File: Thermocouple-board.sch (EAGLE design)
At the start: 82 parts, among them J1 RJ45, J10 1X2-3.5MM, J11 1X2-3.5MM, J12 1X2-3.5MM, J13 1X2-3.5MM, J2 RJ45, J3 1981584-1, J4 2.1MMJACKTHM, J5 ST-LINK, J6 HEADER-1X3, J7 UART, SW1 PUSHBUTTON, SW2 PUSHBUTTON, U1 STM32F042K4, U10 MAX31855, U11 MAX31855, U12 MAX31855, U13 MAX31855, U20 EEPROM-I2C, U21 EEPROM-I2C, U30 ST3485, U31 ST3485, U40 LP298XS, Y1 8MHz

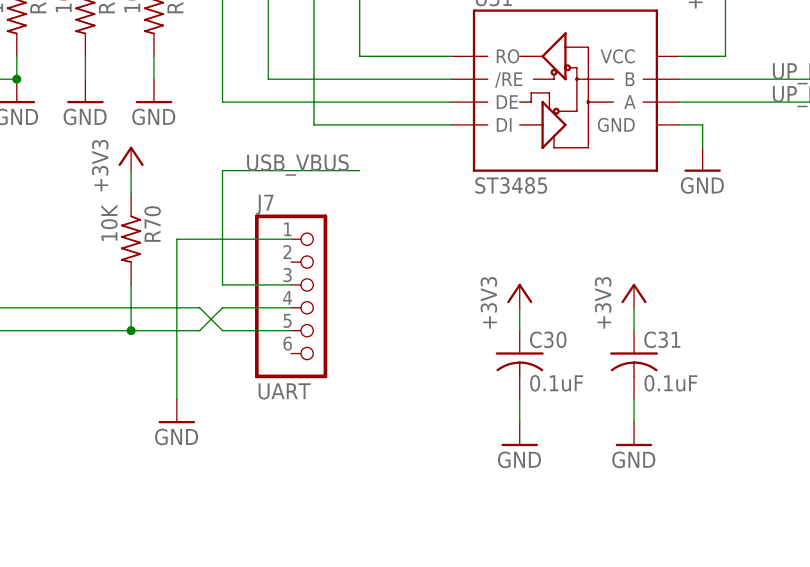
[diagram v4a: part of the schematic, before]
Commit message: Added notes to UART connector
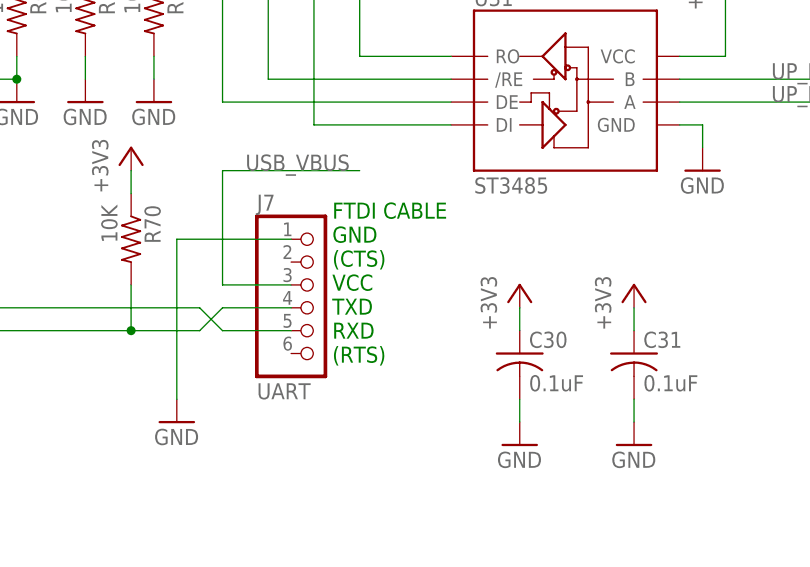
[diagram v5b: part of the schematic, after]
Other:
- note added: "FTDI CABLE GND (CTS) VCC TXD RXD (RTS)"
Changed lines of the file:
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@@
 <text x="53.34" y="63.5" size="1.778" layer="91">POE</text>
 <text x="53.34" y="57.404" size="1.778" layer="91">USB</text>
+<text x="256.032" y="-69.596" size="1.778" layer="91">FTDI CABLE
+GND
+(CTS)
+VCC
+TXD
+RXD
+(RTS)</text>
 </plain>
 <instances>

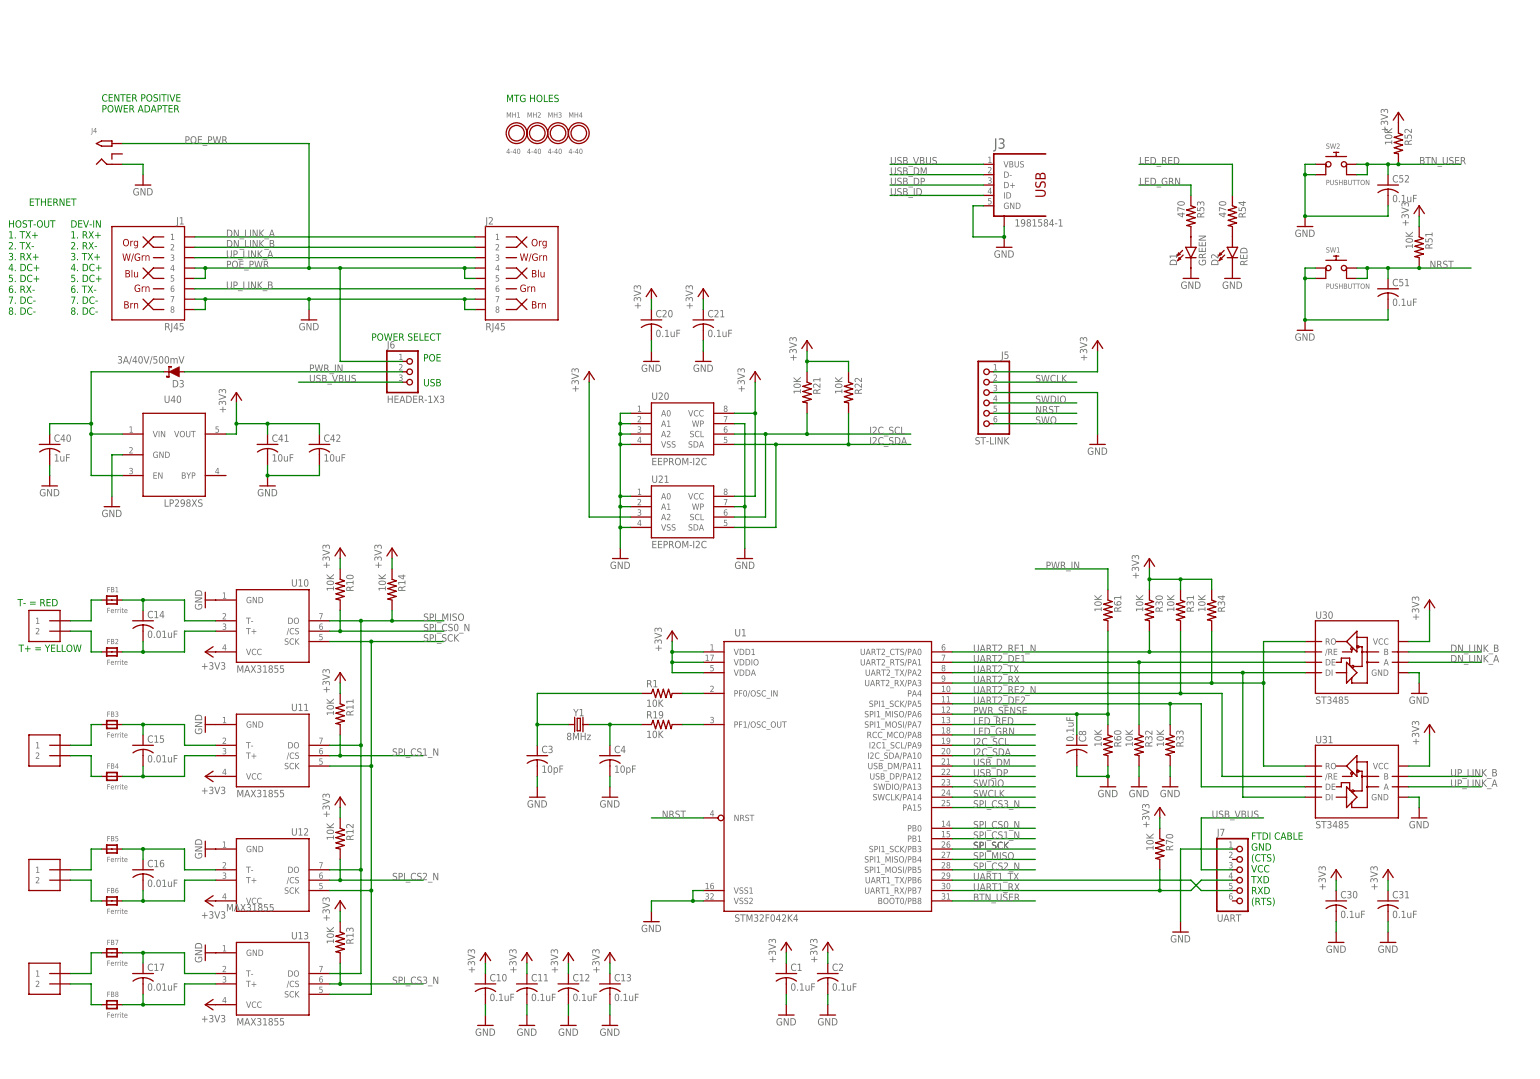
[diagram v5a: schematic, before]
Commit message: Fix pushbutton and SO08. Start of efuse.
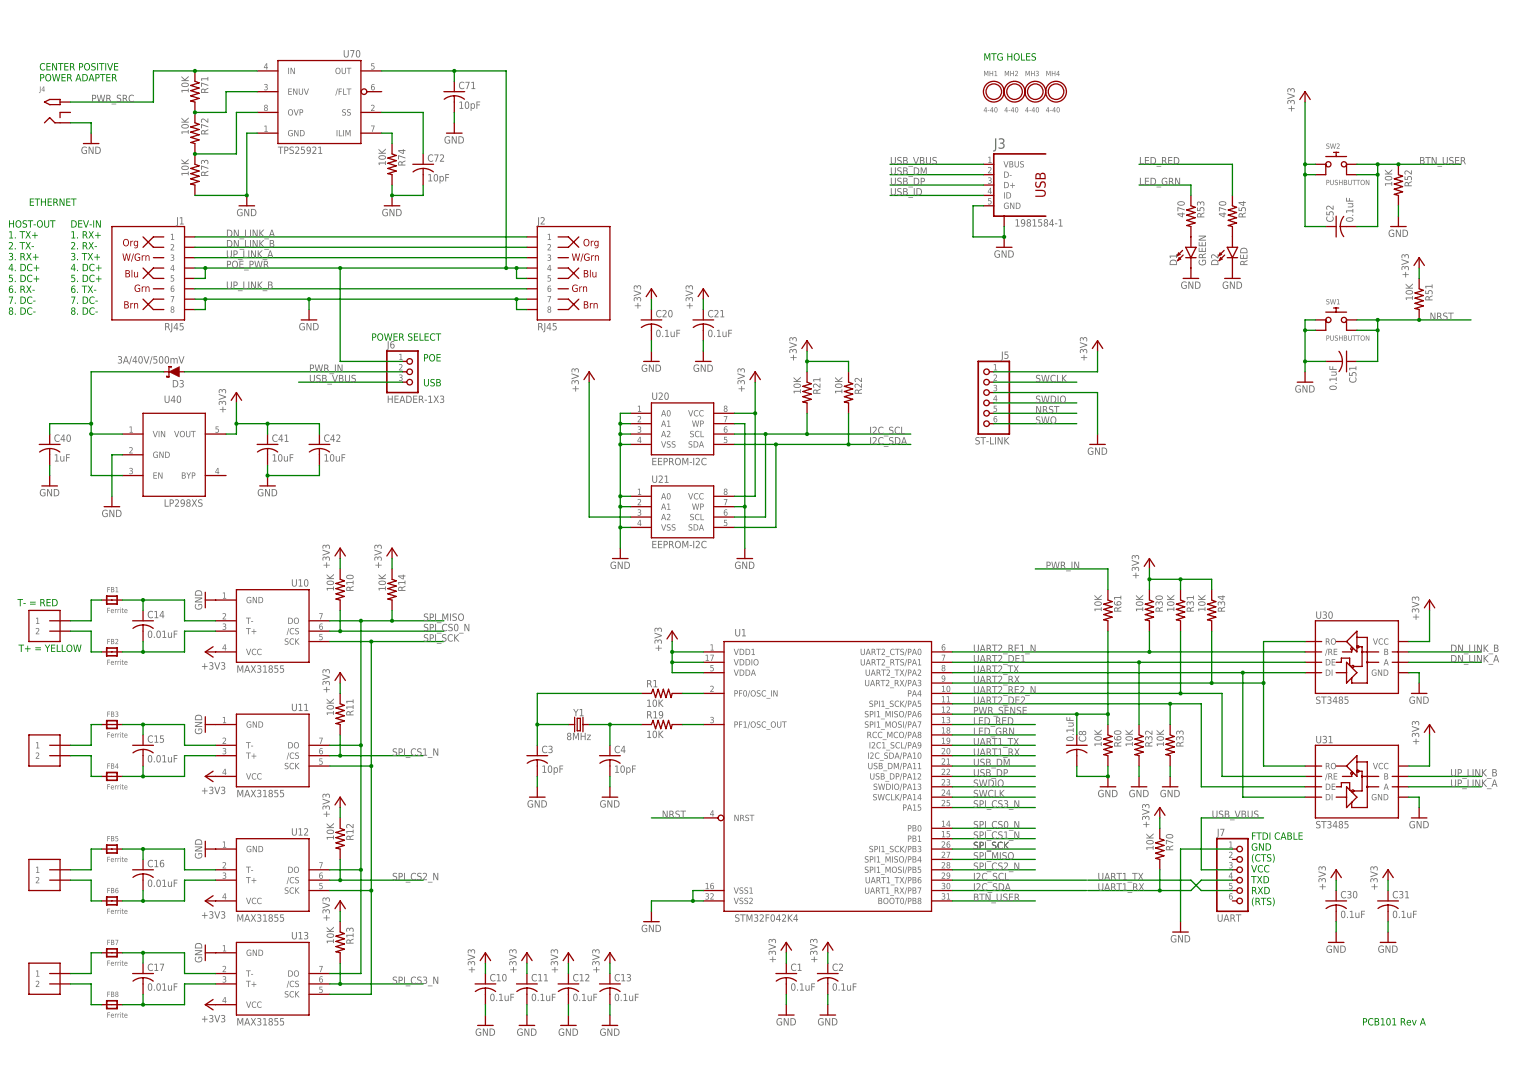
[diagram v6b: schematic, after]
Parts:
- added C71, C72: 10pF, adafruit:C-USC0805K
- added R71, R72, R73, R74: 10K, adafruit:R-US_R0805
- added U70: TPS25921, Thermocouple-board:TPS25921
- U10, U11, U12, U13: device adafruit:MAX6675 -> Thermocouple-board:MAX31855
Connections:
- new net N$23: R71.2, R72.1, U70.ENUV
- new net N$24: R72.2, R73.1, U70.OVP
- new net N$27: R74.1, U70.ILIM
- new net N$28: C72.1, U70.SS
- new net PWR_SRC: J4.TIP, R71.1, U70.IN
- net +3V3: now also C52.1, SW2.P$1, SW2.P$2; no longer R52.1
- net BTN_USER: now also C52.2, R52.1, SW2.P$3; no longer C52.1, R52.2, SW2.P$2
- net GND: now also C71.2, C72.2, R52.2, R73.2, R74.2, SW1.P$2, U70.GND; no longer C52.2, SW1.P$3, SW2.P$1, SW2.P$3
- net I2C_SCL: now also U1.UART1_TX/PB6; no longer U1.I2C1_SCL/PA9
- net I2C_SDA: now also U1.UART1_RX/PB7; no longer U1.I2C_SDA/PA10
- net NRST: now also SW1.P$3; no longer SW1.P$2
- net POE_PWR: now also C71.1, U70.OUT; no longer J4.TIP
- net UART1_RX: now also U1.I2C_SDA/PA10; no longer U1.UART1_RX/PB7
- net UART1_TX: now also U1.I2C1_SCL/PA9; no longer U1.UART1_TX/PB6
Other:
- note added: "PCB101 Rev A"
- moved on the sheet: C51, C52, J2, J4, MH1, MH2, MH3, MH4, R51, R52

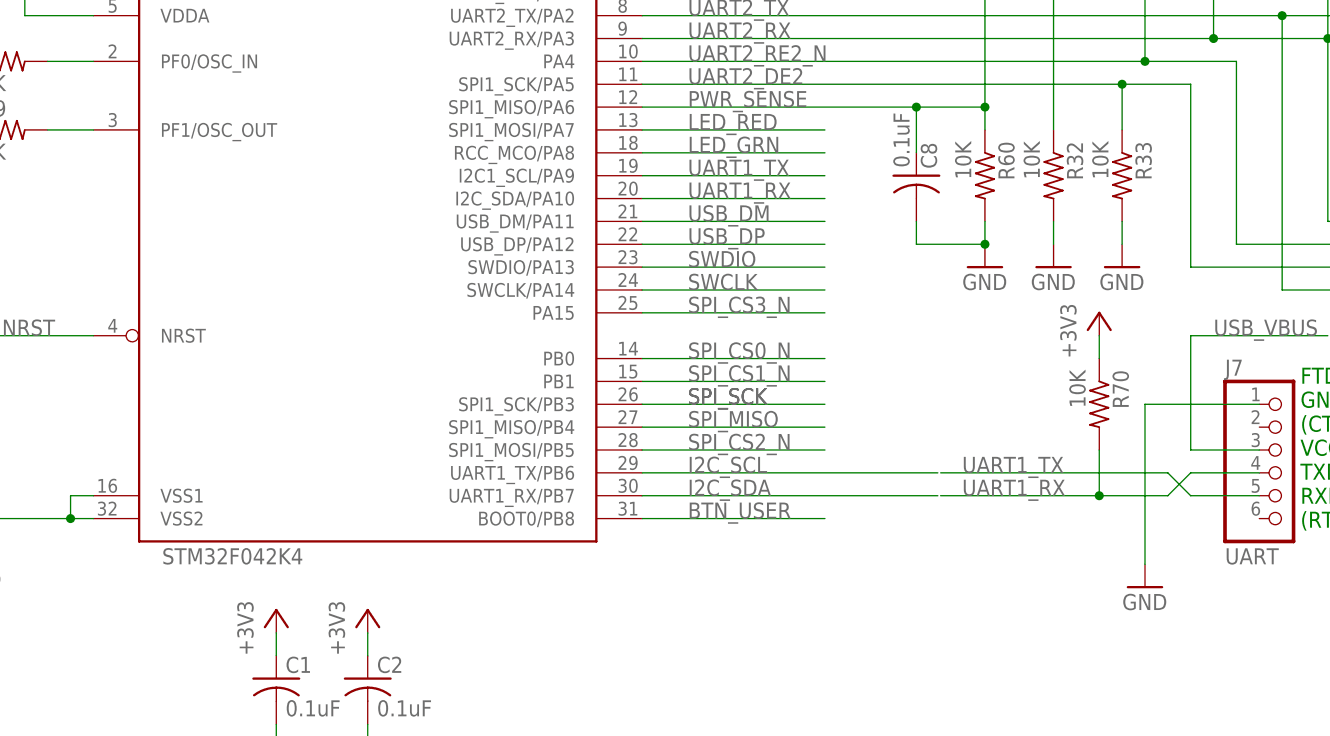
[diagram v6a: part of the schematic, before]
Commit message: RJ-45 rework routing WIP
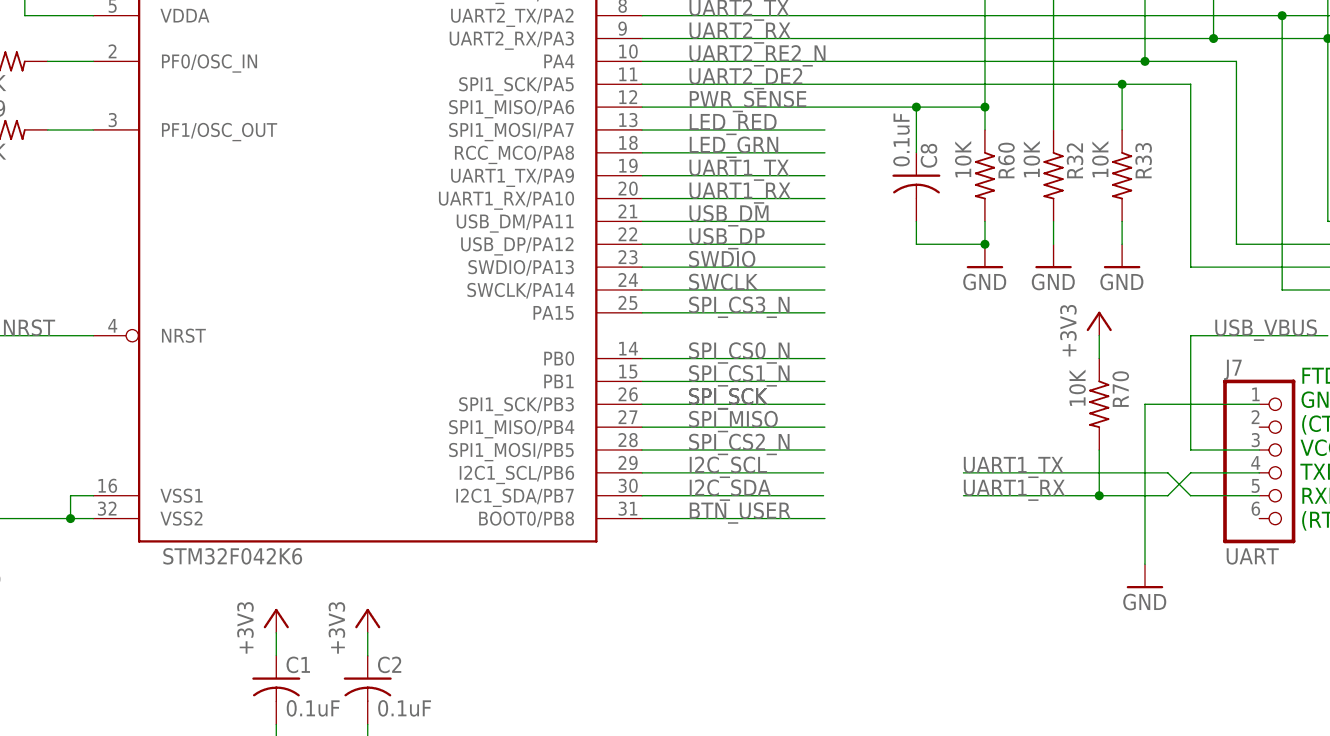
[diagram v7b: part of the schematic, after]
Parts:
- U1: value STM32F042K4 -> STM32F042K6; device Thermocouple-board:STM32F042K4_V01 -> Thermocouple-board:STM32F042K4_V02
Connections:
- net I2C_SCL: now also U1.I2C1_SCL/PB6; no longer U1.UART1_TX/PB6
- net I2C_SDA: now also U1.I2C1_SDA/PB7; no longer U1.UART1_RX/PB7
- net UART1_RX: now also U1.UART1_RX/PA10; no longer U1.I2C_SDA/PA10
- net UART1_TX: now also U1.UART1_TX/PA9; no longer U1.I2C1_SCL/PA9
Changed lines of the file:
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@@
 <part name="+3V31" library="supply1" deviceset="+3V3" device=""/>
 <part name="GND33" library="supply1" deviceset="GND" device=""/>
-<part name="U1" library="Thermocouple-board" deviceset="STM32F042K4_V01" device="" value="STM32F042K4"/>
+<part name="U1" library="Thermocouple-board" deviceset="STM32F042K4_V02" device="" value="STM32F042K6"/>
 <part name="GND12" library="supply1" deviceset="GND" device=""/>
 <part name="R32" library="adafruit" deviceset="R-US_" device="R0805" value="10K"/>
@@
 <pinref part="GND1" gate="1" pin="GND"/>
 <pinref part="U10" gate="G$1" pin="GND"/>
-<pinref part="U10" gate="G$1" pin="GND"/>
 </segment>
 <segment>
 <pinref part="GND5" gate="1" pin="GND"/>
 <pinref part="U11" gate="G$1" pin="GND"/>
-<pinref part="U11" gate="G$1" pin="GND"/>
 </segment>
 <segment>
 <pinref part="GND6" gate="1" pin="GND"/>
-<pinref part="U12" gate="G$1" pin="GND"/>
 <pinref part="U12" gate="G$1" pin="GND"/>
 </segment>
@@
 <pinref part="+3V3" gate="G$1" pin="+3V3"/>
 <pinref part="U10" gate="G$1" pin="VCC"/>
-<pinref part="U10" gate="G$1" pin="VCC"/>
 </segment>
 <segment>
@@
 <pinref part="+3V9" gate="G$1" pin="+3V3"/>
 <pinref part="U11" gate="G$1" pin="VCC"/>
-<pinref part="U11" gate="G$1" pin="VCC"/>
 </segment>
 <segment>
 <pinref part="+3V10" gate="G$1" pin="+3V3"/>
-<pinref part="U12" gate="G$1" pin="VCC"/>
 <pinref part="U12" gate="G$1" pin="VCC"/>
 </segment>
@@
 </segment>
 <segment>
-<pinref part="U1" gate="G$1" pin="UART1_TX/PB6"/>
-<wire x1="215.7476" y1="-63.5" x2="182.88" y2="-63.5" width="0.1524" layer="91"/>
+<pinref part="U1" gate="G$1" pin="I2C1_SCL/PB6"/>
+<wire x1="203.0476" y1="-63.5" x2="182.88" y2="-63.5" width="0.1524" layer="91"/>
 <label x="187.96" y="-63.5" size="1.778" layer="95"/>
 </segment>
@@
 </segment>
 <segment>
-<pinref part="U1" gate="G$1" pin="UART1_RX/PB7"/>
-<wire x1="182.88" y1="-66.04" x2="215.7476" y2="-66.04" width="0.1524" layer="91"/>
+<pinref part="U1" gate="G$1" pin="I2C1_SDA/PB7"/>
+<wire x1="182.88" y1="-66.04" x2="203.0476" y2="-66.04" width="0.1524" layer="91"/>
 <label x="187.96" y="-66.04" size="1.778" layer="95"/>
 </segment>
@@
 <pinref part="J7" gate="A" pin="4"/>
 <wire x1="243.84" y1="-63.5" x2="251.46" y2="-63.5" width="0.1524" layer="91"/>
-<wire x1="216.0524" y1="-66.04" x2="233.68" y2="-66.04" width="0.1524" layer="91"/>
+<wire x1="218.5924" y1="-66.04" x2="233.68" y2="-66.04" width="0.1524" layer="91"/>
 <label x="218.44" y="-66.04" size="1.778" layer="95"/>
 </segment>
@@
 <wire x1="182.88" y1="-33.02" x2="203.2" y2="-33.02" width="0.1524" layer="91"/>
 <label x="187.96" y="-33.02" size="1.778" layer="95"/>
-<pinref part="U1" gate="G$1" pin="I2C_SDA/PA10"/>
+<pinref part="U1" gate="G$1" pin="UART1_RX/PA10"/>
 </segment>
 </net>
@@
 <pinref part="J7" gate="A" pin="5"/>
 <wire x1="243.84" y1="-66.04" x2="251.46" y2="-66.04" width="0.1524" layer="91"/>
-<wire x1="241.3" y1="-63.5" x2="216.0524" y2="-63.5" width="0.1524" layer="91"/>
+<wire x1="241.3" y1="-63.5" x2="218.5924" y2="-63.5" width="0.1524" layer="91"/>
 <label x="218.44" y="-63.5" size="1.778" layer="95"/>
 </segment>
@@
 <wire x1="182.88" y1="-30.48" x2="203.2" y2="-30.48" width="0.1524" layer="91"/>
 <label x="187.96" y="-30.48" size="1.778" layer="95"/>
-<pinref part="U1" gate="G$1" pin="I2C1_SCL/PA9"/>
-</segment>
-</net>
+<pinref part="U1" gate="G$1" pin="UART1_TX/PA9"/>
+</segment>
+</net>

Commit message: Routing WIP
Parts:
- added R40, R41: 120, adafruit:R-US_R0805
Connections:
- net NRST renamed RST_N
- net DN_LINK_A: now also R40.2
- net DN_LINK_B: now also R40.1
- net UP_LINK_A: now also R41.2
- net UP_LINK_B: now also R41.1
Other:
- note added: "DNI"
- note added: "ETHERNET (REF)"
- note added: "MDI (PC) 1. TX+ 2. TX- 3. RX+ 4. DC+ 5. DC+ 6. RX- 7. DC- 8. DC-"
- note added: "MDI-X (HUB) 1. RX+ 2. RX- 3. TX+ 4. DC+ 5. DC+ 6. TX- 7. DC- 8. DC-"
- note removed: "DEV-IN 1. RX+ 2. RX- 3. TX+ 4. DC+ 5. DC+ 6. TX- 7. DC- 8. DC-"
- note removed: "ETHERNET"
- note removed: "HOST-OUT 1. TX+ 2. TX- 3. RX+ 4. DC+ 5. DC+ 6. RX- 7. DC- 8. DC-"
- moved on the sheet: C30, C31, J5, J7, R52, R70, U30, U31
